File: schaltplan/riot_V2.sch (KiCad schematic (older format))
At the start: 15 parts, among them J1 valve_connector_1, J2 battery_connector, J3 valve_connector_2, J4 Conn_01x10_Male_I2C_SPI_plus, Q1 AO3400A, Q2 AO3400A, U1 bme280_board, U2 dcdc_any_to_3v3, U3 dcdc_any_to_5v, U4 ESP32-WROOM-32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

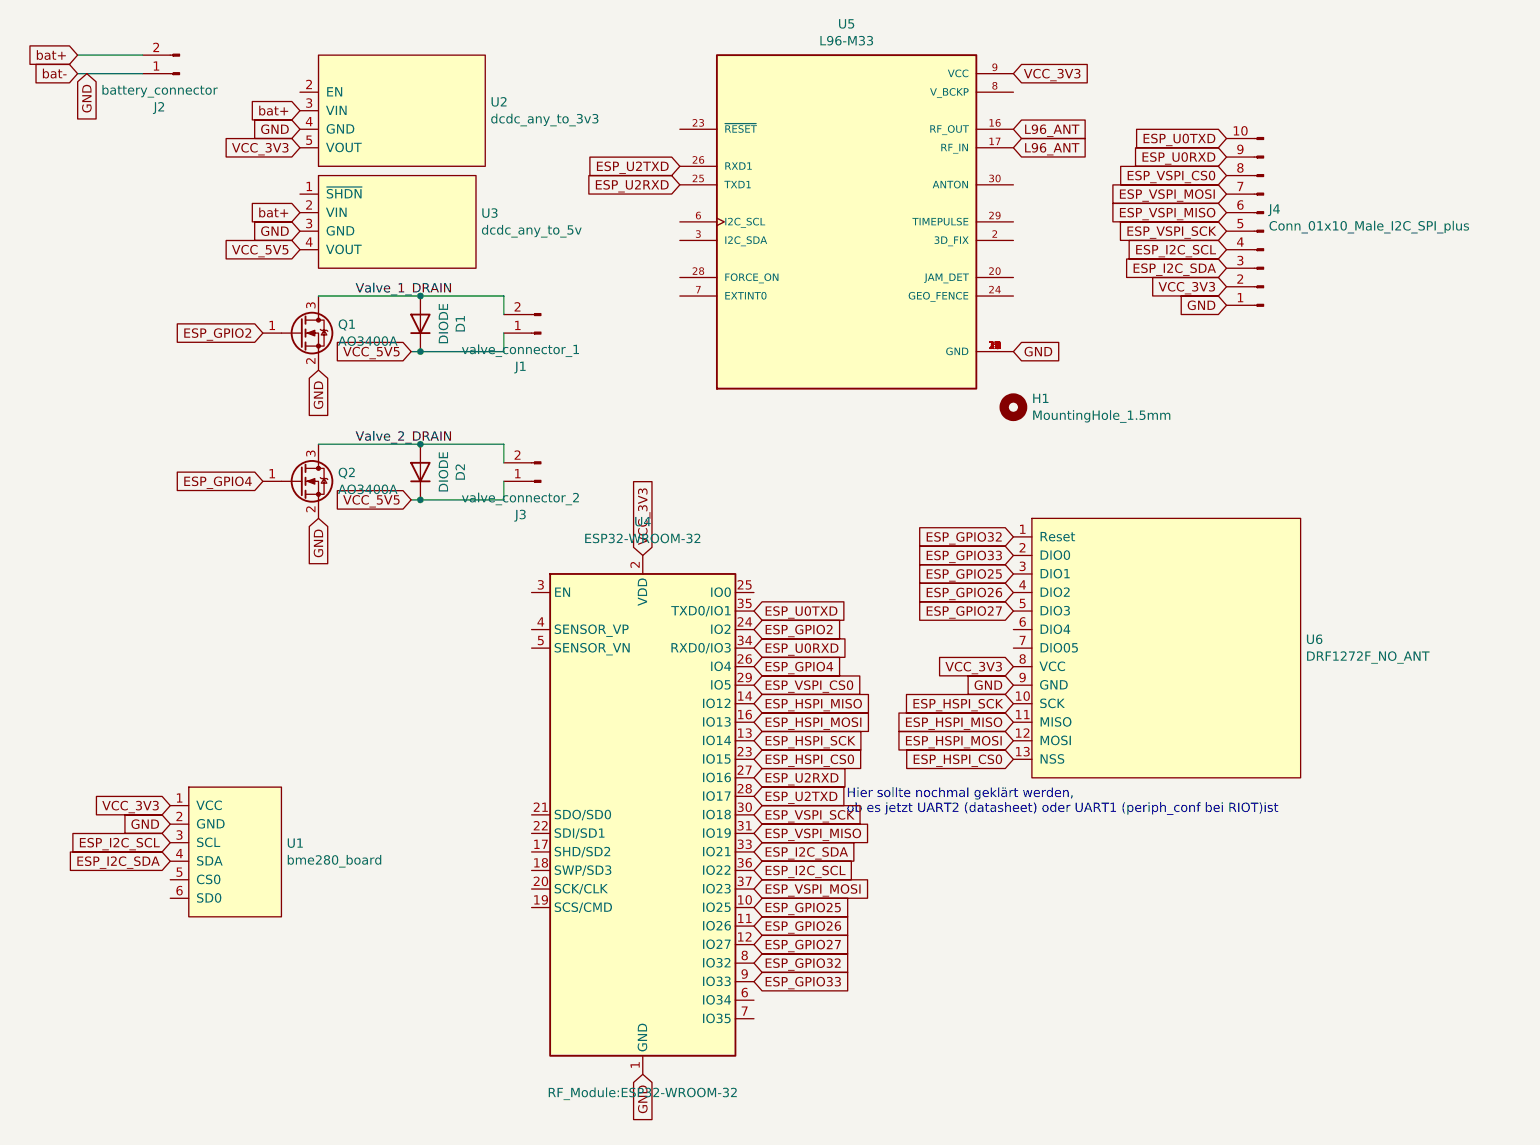
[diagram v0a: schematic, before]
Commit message: Add en and io0 pin to mini-loon board
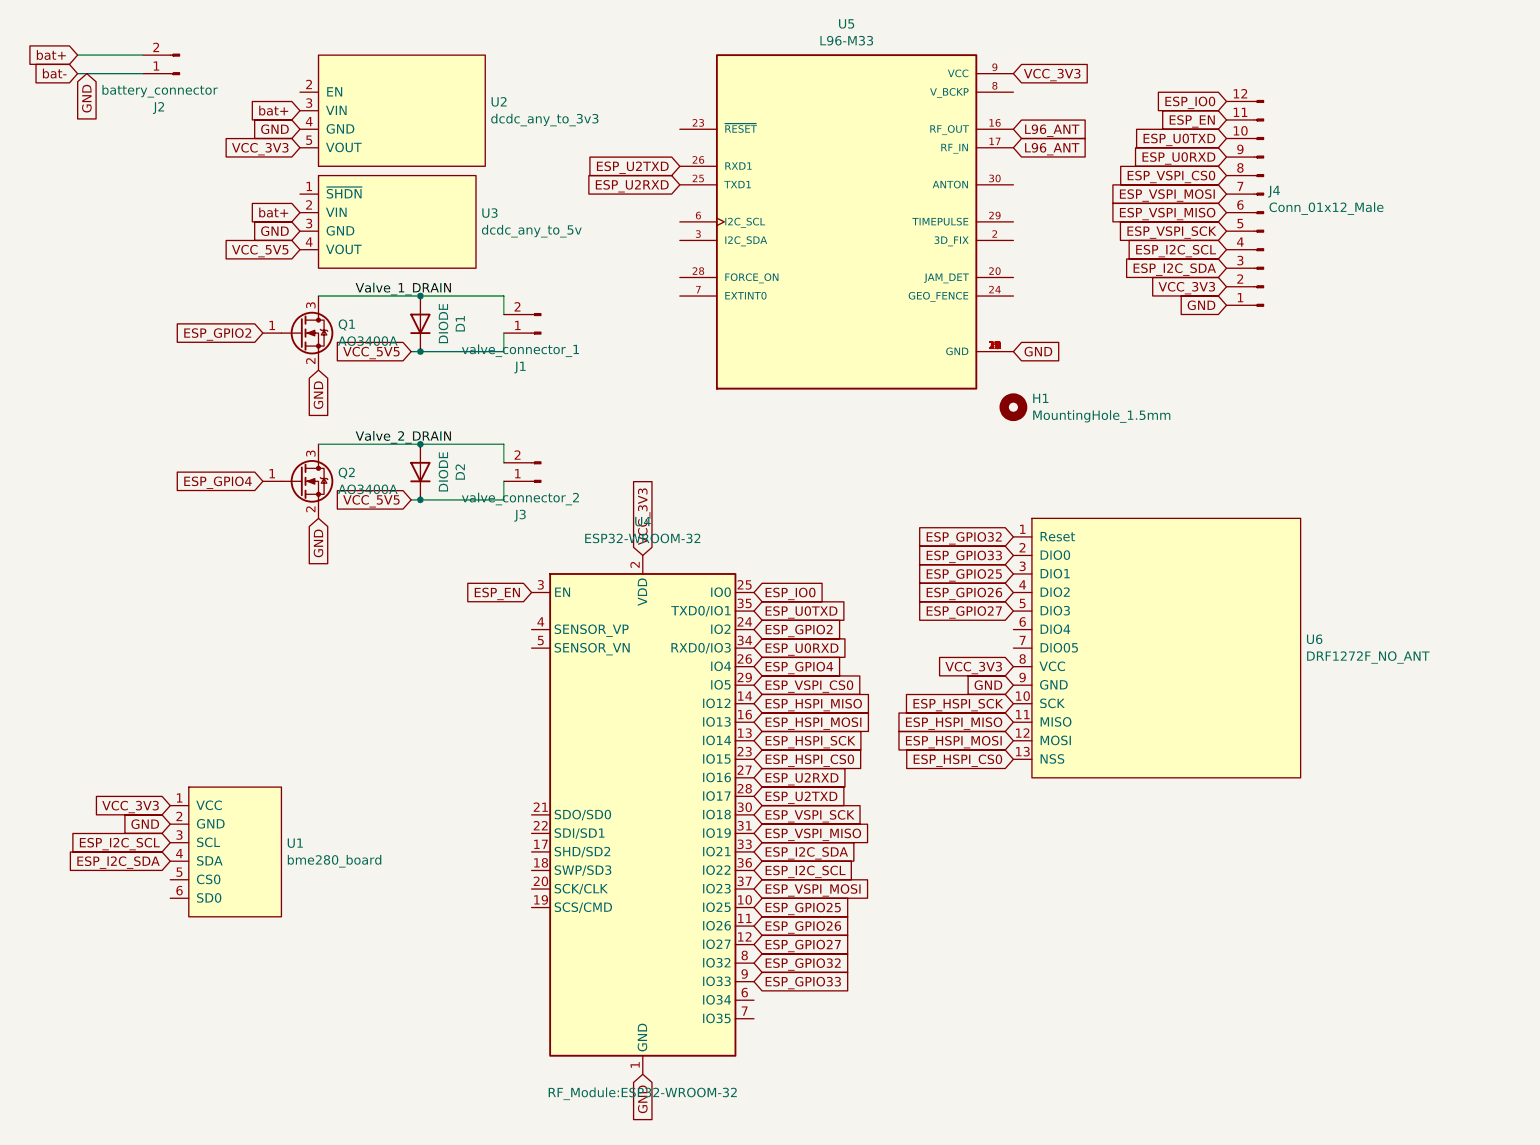
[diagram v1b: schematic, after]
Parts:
- removed J4: Conn_01x10_Male_I2C_SPI_plus, Connector_PinHeader_2.54mm:PinHeader_1x10_P2.54mm_Vertical, symbol Connector:Conn_01x10_Male
- added J4: Conn_01x12_Male, Connector_PinHeader_2.54mm:PinHeader_1x12_P2.54mm_Vertical, symbol Connector:Conn_01x12_Male
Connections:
- net ESP_I2C_SCL: now also J4.4 (Pin_4)
- net ESP_I2C_SDA: now also J4.3 (Pin_3)
- net ESP_U0RXD: now also J4.9 (Pin_9)
- net ESP_U0TXD: now also J4.10 (Pin_10)
- net ESP_VSPI_CS0: now also J4.8 (Pin_8)
- net ESP_VSPI_MISO: now also J4.6 (Pin_6)
- net ESP_VSPI_MOSI: now also J4.7 (Pin_7)
- net ESP_VSPI_SCK: now also J4.5 (Pin_5)
- net GND: now also J4.1 (Pin_1)
- net VCC_3V3: now also J4.2 (Pin_2)
- net ESP_IO0: now reaches U4.25 (IO0)
- net ESP_IO0: now also J4.12 (Pin_12)
- net ESP_EN: now reaches U4.3 (EN)
- net ESP_EN: now also J4.11 (Pin_11)
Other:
- note removed: "Hier sollte nochmal geklärt werden, \nob es jetzt UART2 (datasheet) oder UART1 (periph_conf bei RIOT)ist"
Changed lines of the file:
@@
 Text GLabel 1400 4900 0    50   Input ~ 0
 ESP_I2C_SCL
-Text Notes 5050 4750 0    50   ~ 0
-Hier sollte nochmal geklärt werden, \nob es jetzt UART2 (datasheet) oder UART1 (periph_conf bei RIOT)ist
 Text GLabel 4550 3750 2    50   Input ~ 0
 ESP_GPIO2
@@
 Text GLabel 7100 2000 0    50   Input ~ 0
 GND
-Text GLabel 7100 1900 0    50   Input ~ 0
-VCC_3V3
-Text GLabel 7100 1800 0    50   Input ~ 0
-ESP_I2C_SDA
-Text GLabel 7100 1700 0    50   Input ~ 0
-ESP_I2C_SCL
-Text GLabel 7100 1600 0    50   Input ~ 0
-ESP_VSPI_SCK
-Text GLabel 7100 1500 0    50   Input ~ 0
-ESP_VSPI_MISO
-Text GLabel 7100 1400 0    50   Input ~ 0
-ESP_VSPI_MOSI
-Text GLabel 7100 1300 0    50   Input ~ 0
-ESP_VSPI_CS0
 $Comp
 L Connector:Conn_01x02_Male J3
@@
 Text GLabel 4550 3650 2    50   Input ~ 0
 ESP_U0TXD
-$Comp
-L Connector:Conn_01x10_Male J4
-U 1 1 5FF8A26D
-P 7300 1600
-F 0 "J4" H 7272 1482 50  0000 R CNN
-F 1 "Conn_01x10_Male_I2C_SPI_plus" H 7272 1573 50  0000 R CNN
-F 2 "Connector_PinHeader_2.54mm:PinHeader_1x10_P2.54mm_Vertical" H 7300 1600 50  0001 C CNN
-F 3 "~" H 7300 1600 50  0001 C CNN
-	1    7300 1600
-	-1   0    0    1
-$EndComp
-Text GLabel 7100 1100 0    50   Input ~ 0
-ESP_U0TXD
-Text GLabel 7100 1200 0    50   Input ~ 0
-ESP_U0RXD
 Text GLabel 4550 4750 2    50   Input ~ 0
 ESP_VSPI_SCK
@@
 Text GLabel 5950 1050 2    50   Input ~ 0
 L96_ANT
+Text GLabel 7100 1200 0    50   Input ~ 0
+ESP_U0RXD
+Text GLabel 7100 1100 0    50   Input ~ 0
+ESP_U0TXD
+Text GLabel 7100 1300 0    50   Input ~ 0
+ESP_VSPI_CS0
+Text GLabel 7100 1400 0    50   Input ~ 0
+ESP_VSPI_MOSI
+Text GLabel 7100 1500 0    50   Input ~ 0
+ESP_VSPI_MISO
+Text GLabel 7100 1600 0    50   Input ~ 0
+ESP_VSPI_SCK
+Text GLabel 7100 1700 0    50   Input ~ 0
+ESP_I2C_SCL
+Text GLabel 7100 1800 0    50   Input ~ 0
+ESP_I2C_SDA
+Text GLabel 7100 1900 0    50   Input ~ 0
+VCC_3V3
+$Comp
+L Connector:Conn_01x12_Male J4
+U 1 1 60080608
+P 7300 1500
+F 0 "J4" H 7272 1382 50  0000 R CNN
+F 1 "Conn_01x12_Male" H 7272 1473 50  0000 R CNN
+F 2 "Connector_PinHeader_2.54mm:PinHeader_1x12_P2.54mm_Vertical" H 7300 1500 50  0001 C CNN
+F 3 "~" H 7300 1500 50  0001 C CNN
+	1    7300 1500
+	-1   0    0    1
+$EndComp
+Text GLabel 7100 1000 0    50   Input ~ 0
+ESP_EN
+Text GLabel 7100 900  0    50   Input ~ 0
+ESP_IO0
+Text GLabel 3350 3550 0    50   Input ~ 0
+ESP_EN
+Text GLabel 4550 3550 2    50   Input ~ 0
+ESP_IO0
 $EndSCHEMATC
